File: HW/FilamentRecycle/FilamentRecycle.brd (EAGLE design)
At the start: 100 x 80 mm, 55 parts, among them CON5 MOLEX-53261-0671, IC1 ATMEGA48A-AU, IC2 74HC595D, IC7 FT232RL, Q1 16MHz, Q2 BC847ALT1SMD, Q3 BC847ALT1SMD, X6 PN61729-S

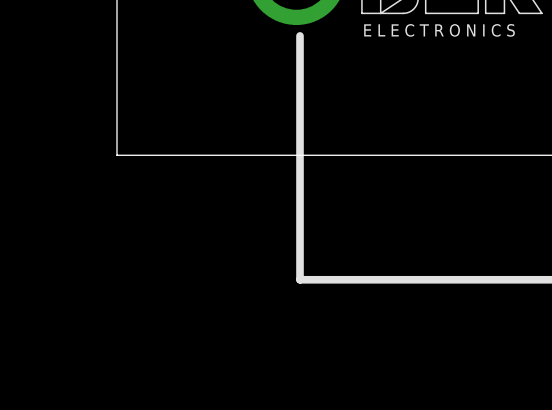
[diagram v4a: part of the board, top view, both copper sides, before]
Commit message: R2R ladder output working via HC595 shift register
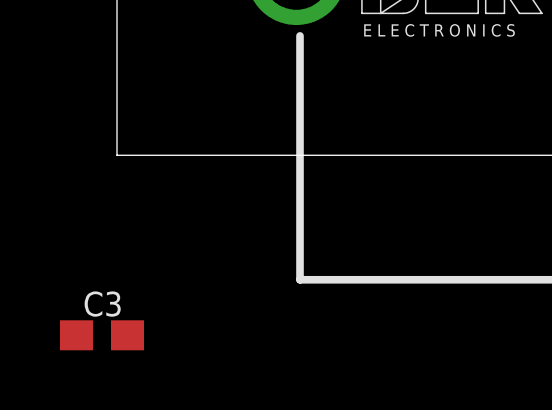
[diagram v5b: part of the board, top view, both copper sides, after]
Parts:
- added C3: 100n, SchlegelAr_Master:C0603
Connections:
- removed net DAC_CLK: IC1.27, IC2.11
- removed net DAC_MISO: IC1.25, IC2.13
- removed net DAC_SS: IC1.26, IC2.12
- removed net VCC: IC2.16
- new net DAC_RCK: IC1.25, IC2.12
- new net DAC_SCK: IC1.26, IC2.11
- net +5V: now also C3.2, IC2.16
- net GND: now also C3.1
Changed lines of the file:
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@@
 <element name="JP7" library="pinhead" package="1X04" value="" x="59.75" y="45.25" rot="R270"/>
 <element name="JP8" library="pinhead" package="1X04" value="" x="58" y="23.5" rot="R270"/>
+<element name="C3" library="SchlegelAr_Master" package="C0603" value="100n" x="-0.5" y="-6"/>
 </elements>
 <signals>
@@
 <contactref element="R26" pad="1"/>
 <contactref element="R27" pad="1"/>
+<contactref element="C3" pad="1"/>
 <wire x1="43.625" y1="70.15" x2="44.895" y2="76.75" width="0" layer="19" extent="16-16"/>
 <wire x1="40.07" y1="66.5734" x2="43.625" y2="70.15" width="0" layer="19" extent="16-16"/>
@@
 <wire x1="28.15" y1="2.5" x2="23.65" y2="8.5" width="0" layer="19" extent="16-16"/>
 <wire x1="5.98" y1="6" x2="13.25" y2="8.71" width="0" layer="19" extent="1-1"/>
+<wire x1="-1.35" y1="-6" x2="5.98" y2="6" width="0" layer="19" extent="1-1"/>
 <wire x1="36.15" y1="32.25" x2="20.85" y2="35.625" width="0" layer="19" extent="16-16"/>
 <wire x1="36.15" y1="29.75" x2="36.15" y2="32.25" width="0" layer="19" extent="16-16"/>
@@
 <wire x1="14.75" y1="56" x2="13.625" y2="57.125" width="0.5" layer="16"/>
 <wire x1="5.55" y1="57.125" x2="13.625" y2="57.125" width="0.5" layer="16"/>
+<contactref element="IC2" pad="16"/>
+<contactref element="C3" pad="2"/>
+<wire x1="31.18" y1="60.4266" x2="38.8" y2="60.4266" width="0" layer="19" extent="16-16"/>
 <wire x1="46.77" y1="51.54" x2="38.8" y2="60.4266" width="0" layer="19" extent="16-16"/>
 <wire x1="46.77" y1="49" x2="46.77" y2="51.54" width="0" layer="19" extent="1-1"/>
@@
 <wire x1="47.77" y1="24.71" x2="47.77" y2="27.25" width="0" layer="19" extent="1-1"/>
 <wire x1="53.27" y1="17.03" x2="47.77" y2="24.71" width="0" layer="19" extent="1-1"/>
-<wire x1="28.025" y1="48" x2="38.8" y2="60.4266" width="0" layer="19" extent="16-16"/>
+<wire x1="28.025" y1="48" x2="31.18" y2="60.4266" width="0" layer="19" extent="16-16"/>
 <wire x1="17.15" y1="46.4574" x2="28.025" y2="48" width="0" layer="19" extent="16-16"/>
 <wire x1="15.55" y1="46.4574" x2="17.15" y2="46.4574" width="0" layer="19" extent="16-16"/>
@@
 <wire x1="25.4" y1="14" x2="24.9" y2="10.75" width="0" layer="19" extent="16-16"/>
 <wire x1="29.85" y1="2.5" x2="25.35" y2="8.5" width="0" layer="19" extent="16-16"/>
+<wire x1="0.35" y1="-6" x2="13.25" y2="10.71" width="0" layer="19" extent="1-1"/>
 </signal>
 <signal name="FTDI_TXD">
@@
 <wire x1="43.625" y1="71.85" x2="45.875" y2="71.85" width="0.8128" layer="16"/>
 </signal>
-<signal name="VCC">
-<contactref element="IC2" pad="16"/>
-</signal>
 <signal name="SS">
 <contactref element="IC1" pad="14"/>
@@
 <wire x1="19.55" y1="55.0426" x2="33.72" y2="60.4266" width="0" layer="19" extent="16-16"/>
 </signal>
-<signal name="DAC_MISO">
-<contactref element="IC2" pad="13"/>
+<signal name="DAC_SCK">
+<contactref element="IC2" pad="11"/>
+<contactref element="IC1" pad="26"/>
+<wire x1="21.0426" y1="52.75" x2="37.53" y2="60.4266" width="0" layer="19" extent="16-16"/>
+</signal>
+<signal name="DAC_RCK">
+<contactref element="IC2" pad="12"/>
 <contactref element="IC1" pad="25"/>
-<wire x1="21.0426" y1="53.55" x2="34.99" y2="60.4266" width="0" layer="19" extent="16-16"/>
-</signal>
-<signal name="DAC_CLK">
-<contactref element="IC2" pad="11"/>
-<contactref element="IC1" pad="27"/>
-<wire x1="21.0426" y1="51.95" x2="37.53" y2="60.4266" width="0" layer="19" extent="16-16"/>
-</signal>
-<signal name="DAC_SS">
-<contactref element="IC2" pad="12"/>
-<contactref element="IC1" pad="26"/>
-<wire x1="21.0426" y1="52.75" x2="36.26" y2="60.4266" width="0" layer="19" extent="16-16"/>
+<wire x1="21.0426" y1="53.55" x2="36.26" y2="60.4266" width="0" layer="19" extent="16-16"/>
 </signal>
 </signals>

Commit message: Eagle brd RC1
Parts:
- removed C12, C8: 100n, SchlegelAr_Master:C0603
- added X1: (no value), con-wago-508:W237-132
- moved C3 71.5 mm to (41.8, 51.6), flipped to the bottom, turned to 90 degrees
- moved C9 37.5 mm to (15.6, 50.0), turned to 270 degrees
- moved JP7 33.7 mm to (51.1, 12.6)
- moved R25 33.2 mm to (29.8, 19.0)
- moved R26 33.2 mm to (29.8, 21.5)
- moved U$7 33.2 mm to (45.2, 20.2)
- moved JP5 33.0 mm to (40.2, 16.4)
- moved C7 27.8 mm to (18.4, 34.5), turned to 180 degrees
- moved R11 18.2 mm to (14.6, 59.4)
- moved S1 18.2 mm to (14.6, 59.4), turned to 270 degrees
- moved JP1 13.6 mm to (20.1, 18.1), turned to 270 degrees
- moved R27 12.8 mm to (30.2, 43.1)
- moved R28 12.8 mm to (30.2, 40.6)
- moved U$14 12.8 mm to (45.2, 41.9)
- moved JP8 12.7 mm to (51.2, 34.2)
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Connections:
- removed net N$31: U$7.GND
- removed net N$40: U$14.GND
- removed net SS: IC1.14
- net +12V: now also X1.1
- net +5V: no longer C12.1, C8.2
- net GND: now also IC2.13, U$14.GND@1, U$7.GND@1, X1.2; no longer C12.2, C8.1
- net MOT_SPINDLE_DIR: now also IC1.1
- net MOT_SPINDLE_STEP: now also IC1.32
- net MOT_WINDING_DIR: now also IC1.28
- net MOT_WINDING_STEP: now also IC1.27
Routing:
- net +5V: track 10.6 -> 235.8 mm, vias 0 -> 9
- net MOT_SPINDLE_DIR: track 0.00 -> 42.0 mm
- net !RESET: track 0.00 -> 40.7 mm, vias 0 -> 3
- net MOT_SPINDLE_STEP: track 0.00 -> 40.0 mm
- net +12V: track 0.00 -> 31.5 mm
- net FTDI_RXD: track 0.00 -> 25.5 mm, vias 0 -> 2
- net NTC_SIG: track 0.00 -> 24.8 mm
- net MOT_WINDING_DIR: track 0.00 -> 23.6 mm
- net FTDI_TXD: track 0.00 -> 23.4 mm, vias 0 -> 2
- net MOT_WINDING_STEP: track 0.00 -> 22.1 mm
- net DAC_SCK: track 0.00 -> 22.1 mm
- net DAC_RCK: track 0.00 -> 20.6 mm
- net CALIPER_DAT_3V3: track 2.90 -> 22.7 mm
- net CALIPER_CLK_3V3: track 2.04 -> 21.0 mm
- net DAC_MOSI: track 0.00 -> 18.1 mm
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- added copper zone on layer 16, net +5V
- added copper zone on layer 1, net GND
- added copper zone on layer 16, net GND
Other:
- board size 100 x 80 mm -> 54 x 73 mm

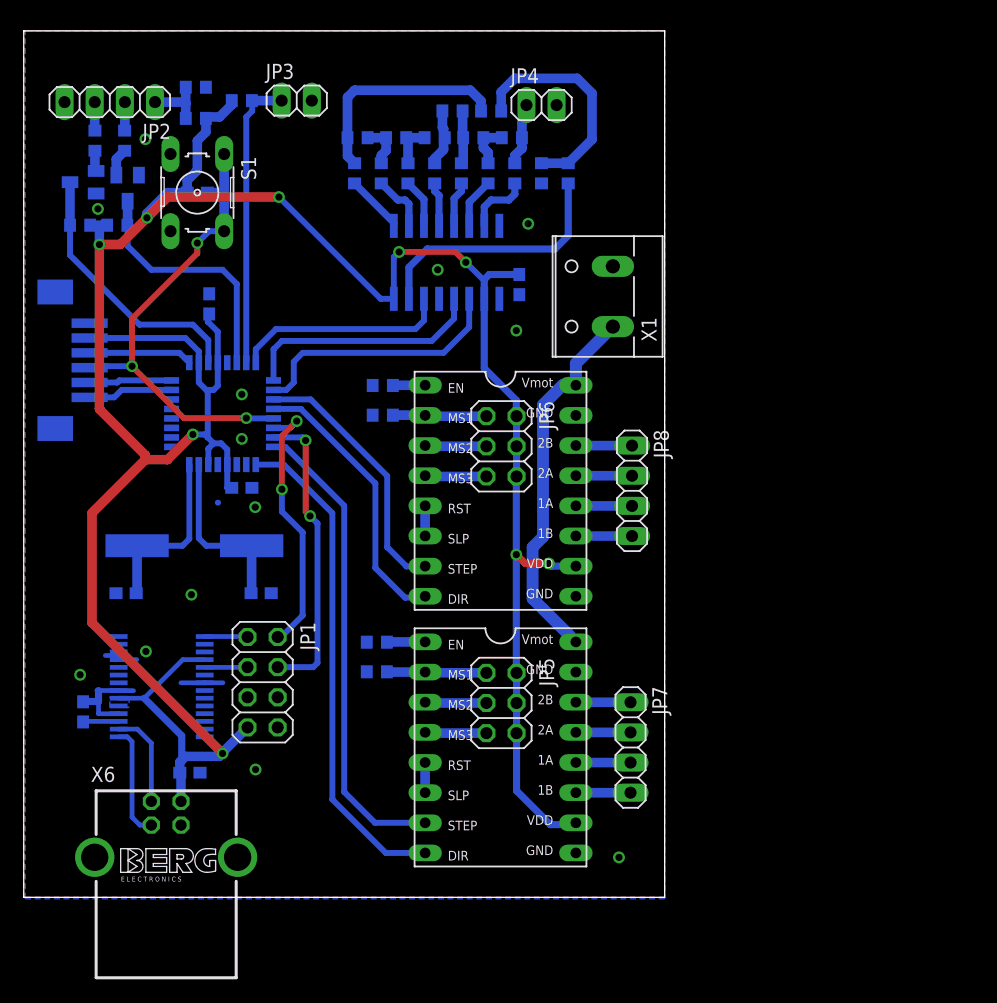
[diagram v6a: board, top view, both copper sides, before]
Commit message: First tests of target hardware. DAC, Caliper and thermistor working
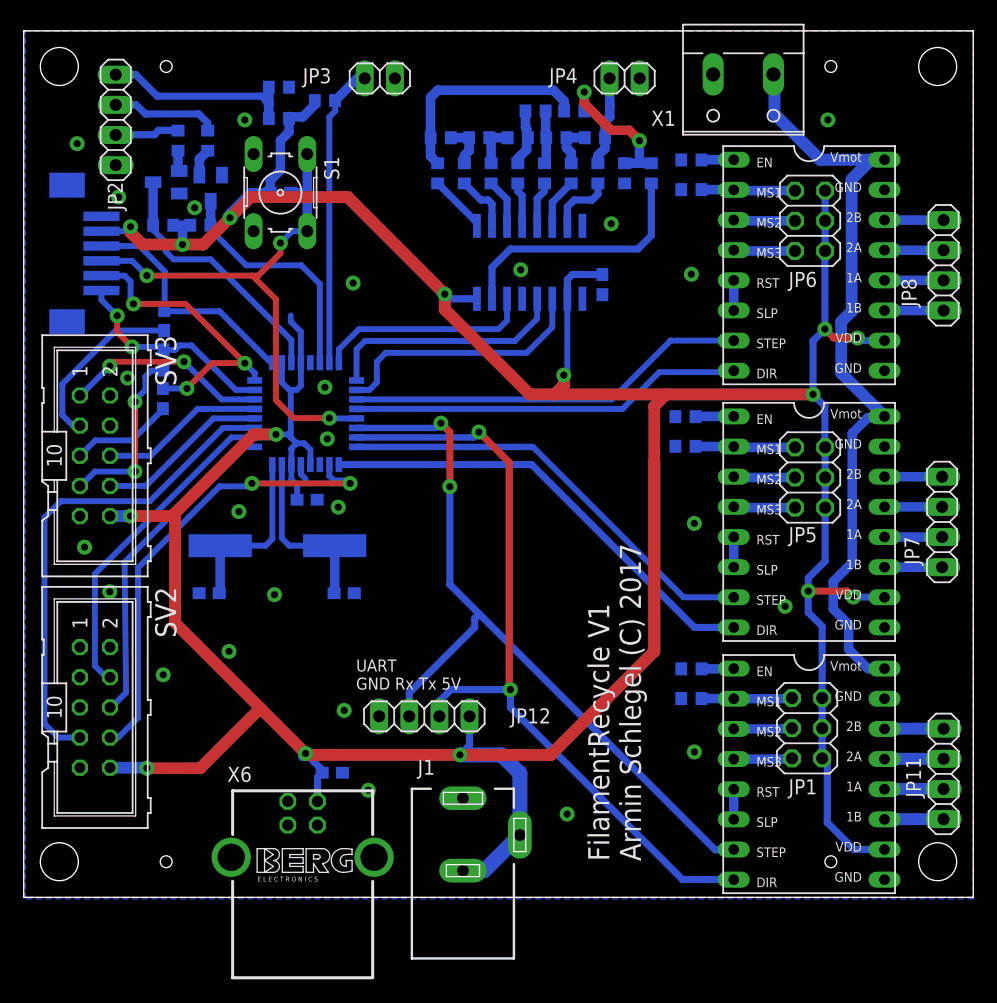
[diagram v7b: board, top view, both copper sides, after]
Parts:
- removed C11, C9: 100n, SchlegelAr_Master:C0603
- removed IC7: FT232RL, SchlegelAr_Master:SSOP28
- added J1: DCJ0202, con-jack:DCJ0202
- added JP11, JP12: (no value), pinhead:1X04
- added R29, R30, R31: 10k, SchlegelAr_Master:R0603
- added R32: 10k, rcl:R0603
- added R33: 100k, rcl:R0603
- added SV2, SV3: (no value), con-harting-ml:ML10
- added U$9: A4988BREAKOUT, RepRapjr:A4988BREAKOUT
- JP1: device pinhead:2X04 -> pinhead:2X03
- moved JP1 46.0 mm to (66.0, 14.2)
- moved JP7 32.4 mm to (77.4, 31.6)
- moved JP8 32.4 mm to (77.5, 53.2)
- moved JP5 32.2 mm to (66.2, 35.4)
- moved JP6 32.2 mm to (66.2, 57.0)
- moved R25 32.2 mm to (55.8, 38.0)
- moved R26 32.2 mm to (55.8, 40.5)
- moved R27 32.2 mm to (56.2, 62.1)
- moved R28 32.2 mm to (56.2, 59.6)
- moved U$14 32.2 mm to (71.2, 60.9)
- moved U$7 32.2 mm to (71.2, 39.2)
- moved X1 21.5 mm to (60.6, 68.7), turned to 180 degrees
- moved C6 12.0 mm to (26.0, 10.5)
- moved X6 11.5 mm to (23.5, 3.38)
- moved CON5 9.06 mm to (4.00, 54.2)
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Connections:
- net N$1 renamed CLKP
- net N$2 renamed CLKN
- removed net FTDI_3V3OUT: C11.1, IC7.17
- removed net FTDI_RXD: IC1.31, JP1.4
- removed net FTDI_TXD: IC1.30, JP1.2
- removed net USB_D+: IC7.15, X6.3
- removed net USB_D-: IC7.16, X6.2
- new net !MOT_WINDING_EN1: R32.2, U$9.EN
- new net DISP_D4: R29.2, SV3.7
- new net DISP_D5: R30.2, SV3.5
- new net DISP_D6: R31.2, SV3.3
- new net DISP_D7: IC1.14, SV3.1
- new net DISP_EN: IC1.13, SV3.6
- new net DISP_RS: IC1.12, SV3.8
- new net ENCODER_A: IC1.2, SV2.8
- new net ENCODER_B: IC1.10, SV2.4
- new net ENCODER_BTN: IC1.9, SV2.6
- new net LED: IC1.11, SV2.7
- new net MOT_REEL_DIR/UART_TXD: IC1.31, JP12.2, U$9.DIR
- new net MOT_REEL_STEP/UART_RXD: IC1.30, JP12.3, U$9.STEP
- new net N$1: JP1.5, U$9.MS3
- new net N$2: JP1.1, R33.1, U$9.MS1
- new net N$31: JP11.2, U$9.2A
- new net N$40: JP11.3, U$9.1A
- new net N$41: JP11.4, U$9.1B
- new net N$42: U$9.RST, U$9.SLP
- net +12V: now also U$9.VMOT
- net +5V: now also J1.2, J1.3, JP1.2, JP1.4, JP1.6, JP12.1, SV2.10, SV3.10, U$9.VDD; no longer C9.2, IC7.19, IC7.20, IC7.4, JP1.7, JP1.8
- net GND: now also J1.1, JP12.4, R32.1, R33.2, SV2.2, SV3.2, U$9.GND@0, U$9.GND@1; no longer C11.2, C9.1, IC7.18, IC7.21, IC7.25, IC7.26, IC7.7, JP1.5, JP1.6
- net MISO: now also R30.1
- net MOSI: now also R29.1
- net N$5: now also JP1.3, U$9.MS2; no longer IC7.1, JP1.1
- net N$8: now also JP11.1, U$9.2B; no longer IC7.5, JP1.3
- net SCK: now also R31.1
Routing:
- net +5V: track 235.8 -> 340.4 mm, vias 9 -> 15
- net MOT_REEL_DIR/UART_TXD: track 0.00 -> 67.3 mm, vias 0 -> 2
- net MOT_REEL_STEP/UART_RXD: track 0.00 -> 65.4 mm, vias 0 -> 2
- net LED: track 0.00 -> 41.7 mm
- net ENCODER_A: track 0.00 -> 39.5 mm, vias 0 -> 2
- net +12V: track 31.5 -> 64.8 mm
- net ENCODER_BTN: track 0.00 -> 27.8 mm
- net ENCODER_B: track 0.00 -> 27.6 mm
- net FTDI_RXD: track 25.5 -> 0.00 mm, vias 2 -> 0
- net FTDI_TXD: track 23.4 -> 0.00 mm, vias 2 -> 0
- net MISO: track 6.98 -> 25.7 mm, vias 0 -> 3
- net DISP_D7: track 0.00 -> 17.2 mm, vias 0 -> 2
- net DISP_D4: track 0.00 -> 15.3 mm, vias 0 -> 2
- net DISP_D6: track 0.00 -> 14.9 mm
- net DISP_RS: track 0.00 -> 14.5 mm
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- removed copper zone on layer 16, net +5V
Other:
- board size 54 x 73 mm -> 80 x 73 mm
- board text added: "FilamentRecycle V1 Armin Schlegel (C) 2017"
- board text added: "UART GND Rx Tx 5V"

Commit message: Added LCD library, Fixed hw bug (series resistors for LCD removed)
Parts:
- R29, R30, R31: value 10k -> 0R
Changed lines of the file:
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@@
 <attribute name="OC_FARNELL" value="unknown" x="6" y="16" size="1.778" layer="27" rot="R270" display="off"/>
 </element>
-<element name="R29" library="SchlegelAr_Master" package="R0603" value="10k" x="11.775" y="45.275" smashed="yes" rot="MR270">
+<element name="R29" library="SchlegelAr_Master" package="R0603" value="0R" x="11.775" y="45.275" smashed="yes" rot="MR270">
 <attribute name="NAME" x="11.14" y="46.66" size="0.8128" layer="26" rot="MR270"/>
 <attribute name="VALUE" x="13.68" y="45.91" size="0.8128" layer="28" rot="MR270"/>
 </element>
-<element name="R30" library="SchlegelAr_Master" package="R0603" value="10k" x="11.725" y="42.025" rot="MR270"/>
-<element name="R31" library="SchlegelAr_Master" package="R0603" value="10k" x="11.825" y="48.6" rot="MR270"/>
+<element name="R30" library="SchlegelAr_Master" package="R0603" value="0R" x="11.725" y="42.025" rot="MR270"/>
+<element name="R31" library="SchlegelAr_Master" package="R0603" value="0R" x="11.825" y="48.6" rot="MR270"/>
 <element name="JP1" library="pinhead" package="2X03" value="" x="66" y="14.25" smashed="yes" rot="R270">
 <attribute name="NAME" x="64.44" y="8.675" size="1.27" layer="25" ratio="10"/>
